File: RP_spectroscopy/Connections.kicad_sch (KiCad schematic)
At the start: 6 parts, among them J1 Extension connector 1, J2 Extension connector 2, J3 Conn_Coaxial, J4 Conn_Coaxial, J5 Conn_Coaxial, J6 Conn_Coaxial

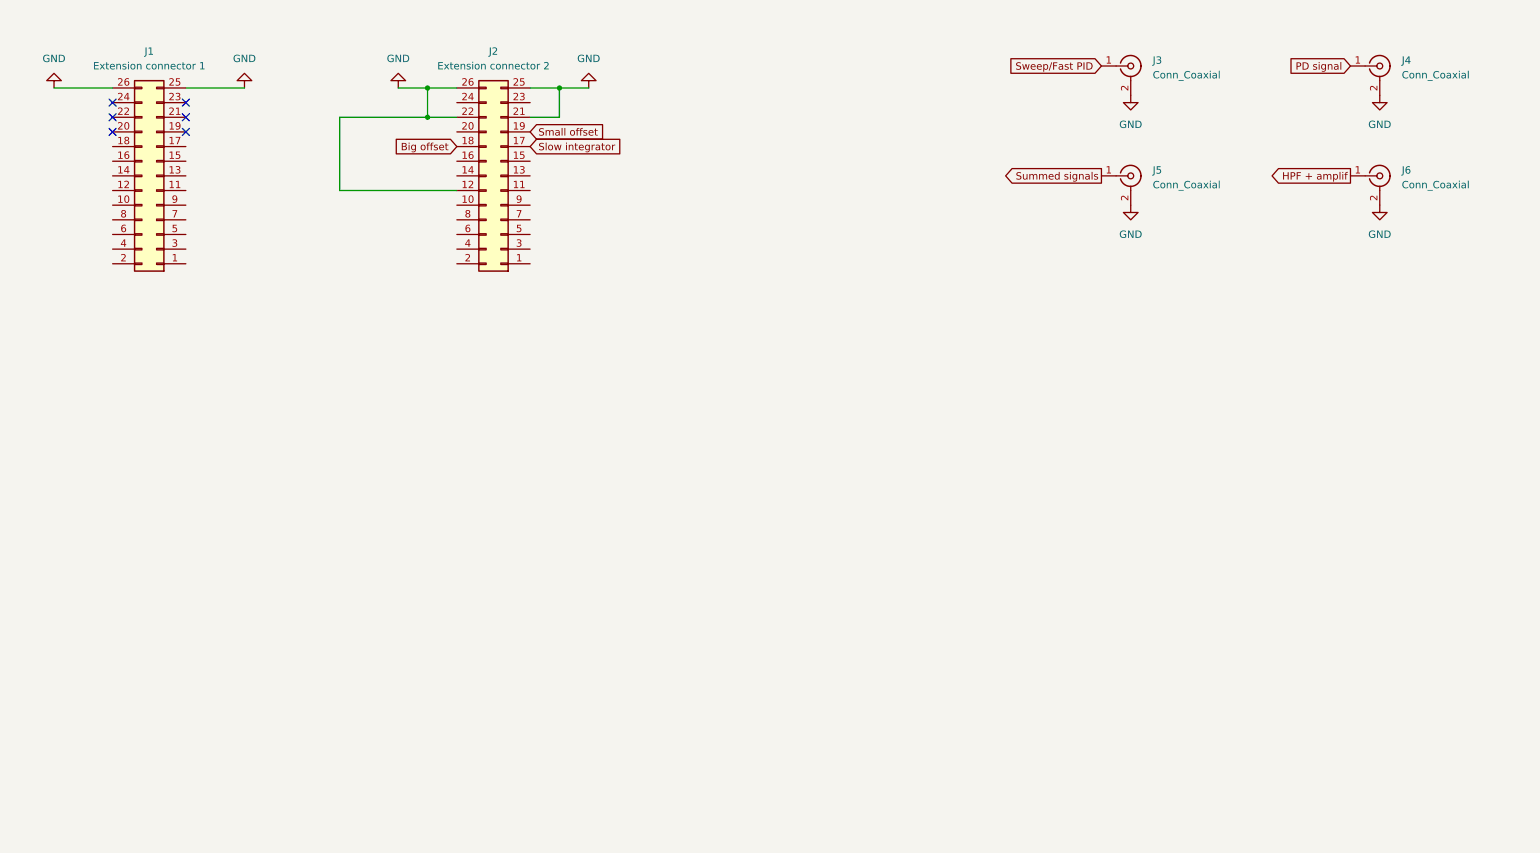
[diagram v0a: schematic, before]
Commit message: Almost finished the summator. Added also some components in the connectors schematic
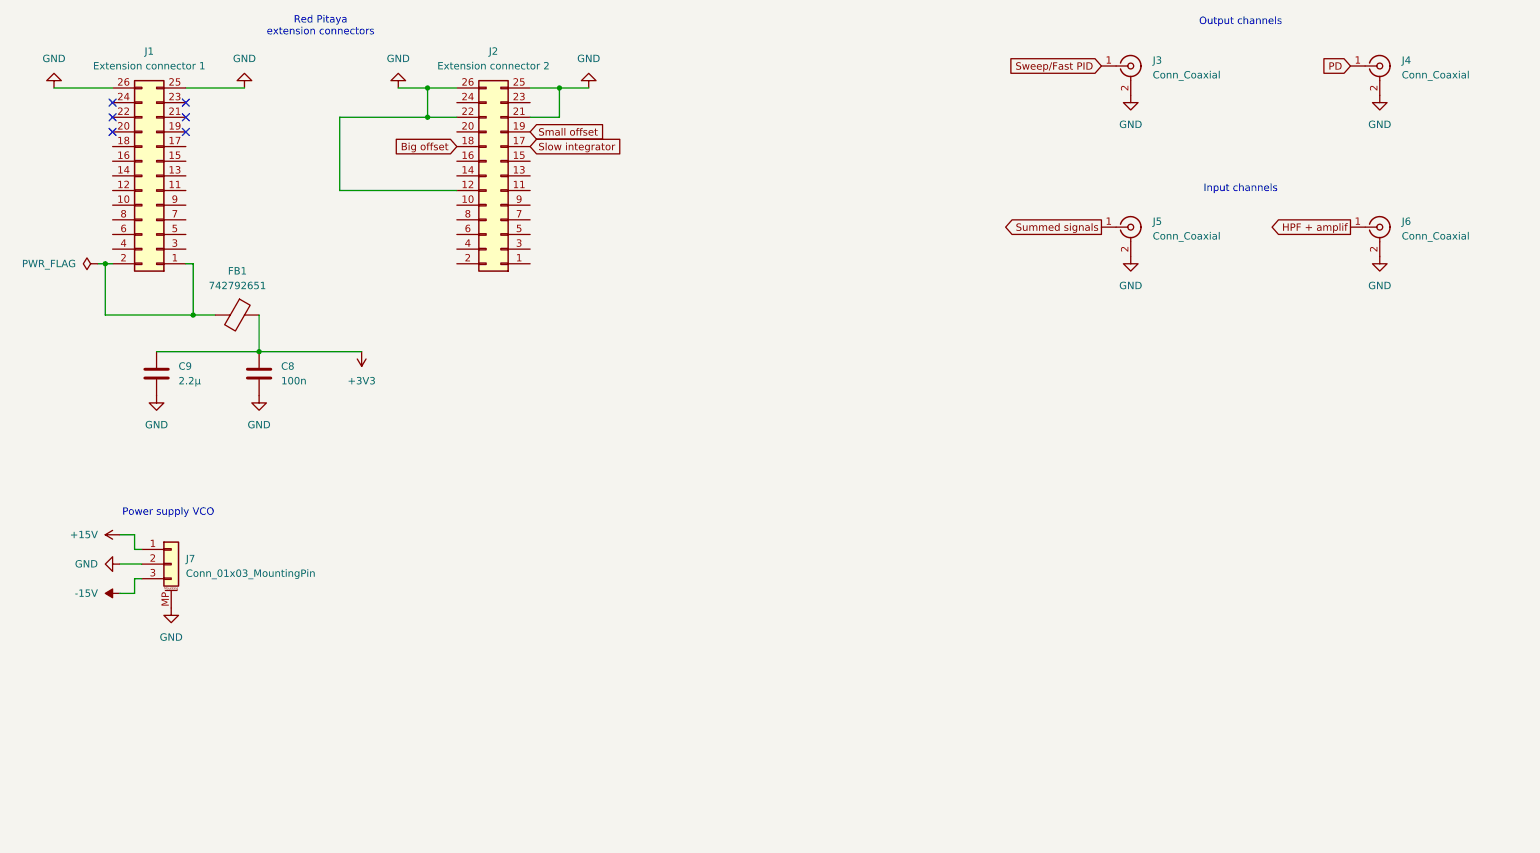
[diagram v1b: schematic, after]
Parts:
- added C8: 100n, symbol Device:C
- added C9: 2.2µ, symbol Device:C
- added FB1: 742792651, symbol Device:FerriteBead
- added J7: Conn_01x03_MountingPin, symbol Connector_Generic_MountingPin:Conn_01x03_MountingPin
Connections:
- net GND: now also C8.2, C9.2, J7.2 (Pin_2), J7.MP (MountPin)
- net at J1.1 (Pin_1): now also J1.2 (Pin_2), FB1.2
- net PD signal renamed PD
- new net +15V: J7.1 (Pin_1)
- new net +3V3: C8.1, C9.1, FB1.1
- new net -15V: J7.3 (Pin_3)
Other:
- note added: "Input channels"
- note added: "Output channels"
- note added: "Power supply VCO"
- note added: "Red Pitaya extension connectors"
- moved on the sheet: J5, J6

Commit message: Continued with the connection scheet
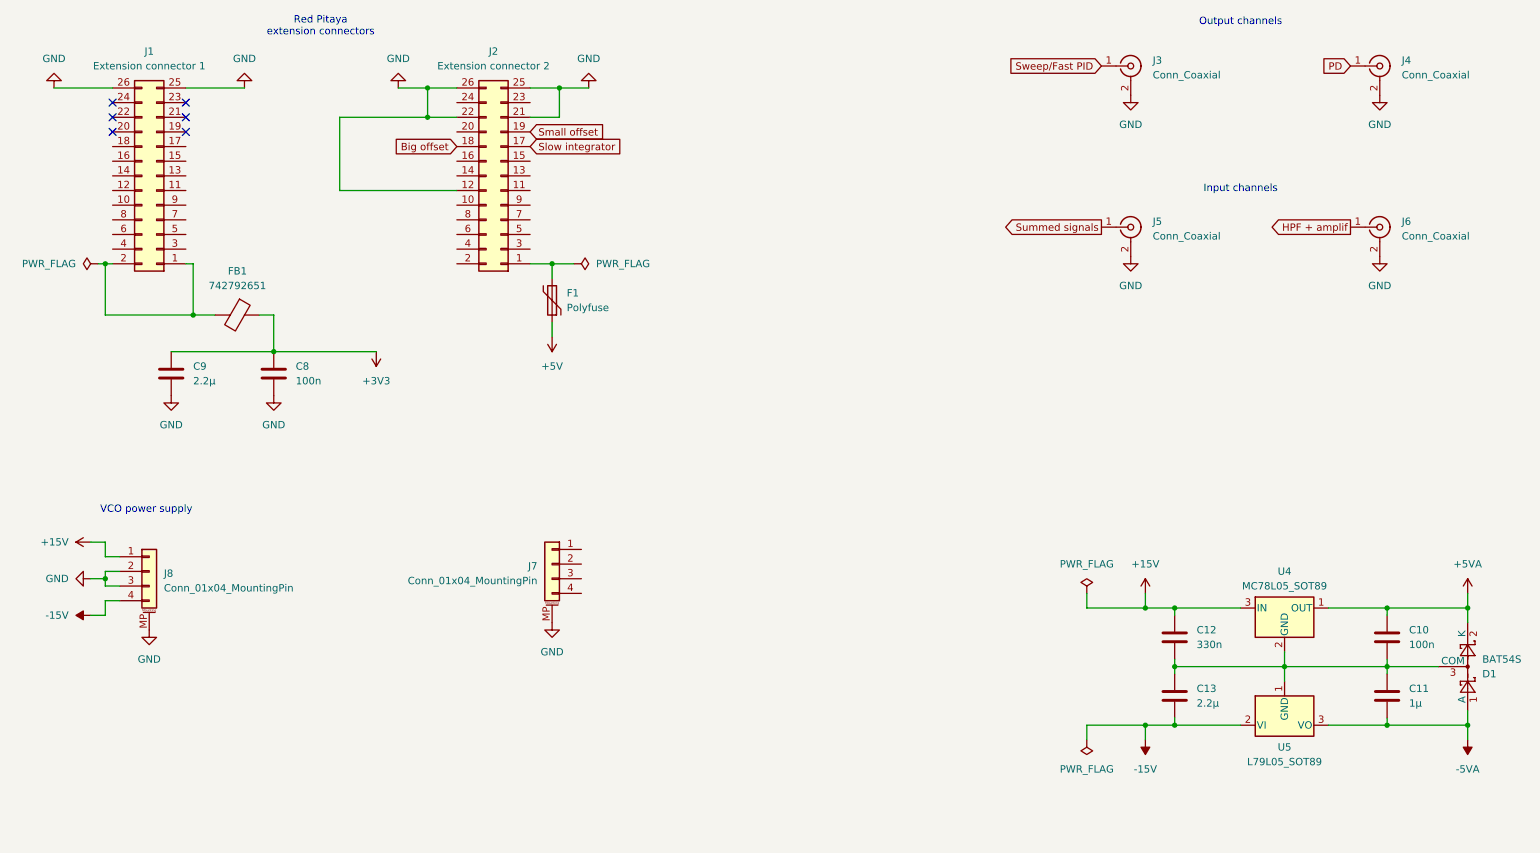
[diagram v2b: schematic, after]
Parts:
- removed J7: Conn_01x03_MountingPin, symbol Connector_Generic_MountingPin:Conn_01x03_MountingPin
- added C10: 100n, symbol Device:C
- added C11: 1µ, symbol Device:C
- added C12: 330n, symbol Device:C
- added C13: 2.2µ, symbol Device:C
- added D1: BAT54S, Package_TO_SOT_SMD:SOT-23, symbol Diode:BAT54S
- added F1: Polyfuse, symbol Device:Polyfuse
- added J7: Conn_01x04_MountingPin, symbol Connector_Generic_MountingPin:Conn_01x04_MountingPin
- added J8: Conn_01x04_MountingPin, Connector_Molex:Molex_PicoBlade_53261-0471_1x04-1MP_P1.25mm_Horizontal, symbol Connector_Generic_MountingPin:Conn_01x04_MountingPin
- added U4: MC78L05_SOT89, Package_TO_SOT_SMD:SOT-89-3_Handsoldering, symbol Regulator_Linear:MC78L05_SOT89
- added U5: L79L05_SOT89, Package_TO_SOT_SMD:SOT-89-3_Handsoldering, symbol Regulator_Linear:L79L05_SOT89
- J1, J2: footprint (none) -> Connector_PinSocket_2.54mm:PinSocket_2x13_P2.54mm_Vertical_SMD
- J3, J4, J5, J6: footprint (none) -> Connector_Coaxial:SMA_Molex_73251-1153_EdgeMount_Horizontal
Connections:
- net +15V: now also C12.1, J8.1 (Pin_1), U4.3 (IN)
- net -15V: now also C13.2, J8.4 (Pin_4), U5.2 (VI)
- net GND: now also J7.MP (MountPin), J8.2 (Pin_2), J8.3 (Pin_3), J8.MP (MountPin)
- net at J2.1 (Pin_1): now also F1.2
- new net: C10.2, C11.1, C12.2, C13.1, D1.3 (COM), U4.2 (GND), U5.1 (GND)
- new net +5V: F1.1
- new net +5VA: C10.1, D1.2 (K), U4.1 (OUT)
- new net -5VA: C11.2, D1.1 (A), U5.3 (VO)
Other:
- note added: "VCO power supply"
- note removed: "Power supply VCO"
- moved on the sheet: C8, C9

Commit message: Added components to the power supply branch. Implemented the Sallen-Key filter + amplification branch.
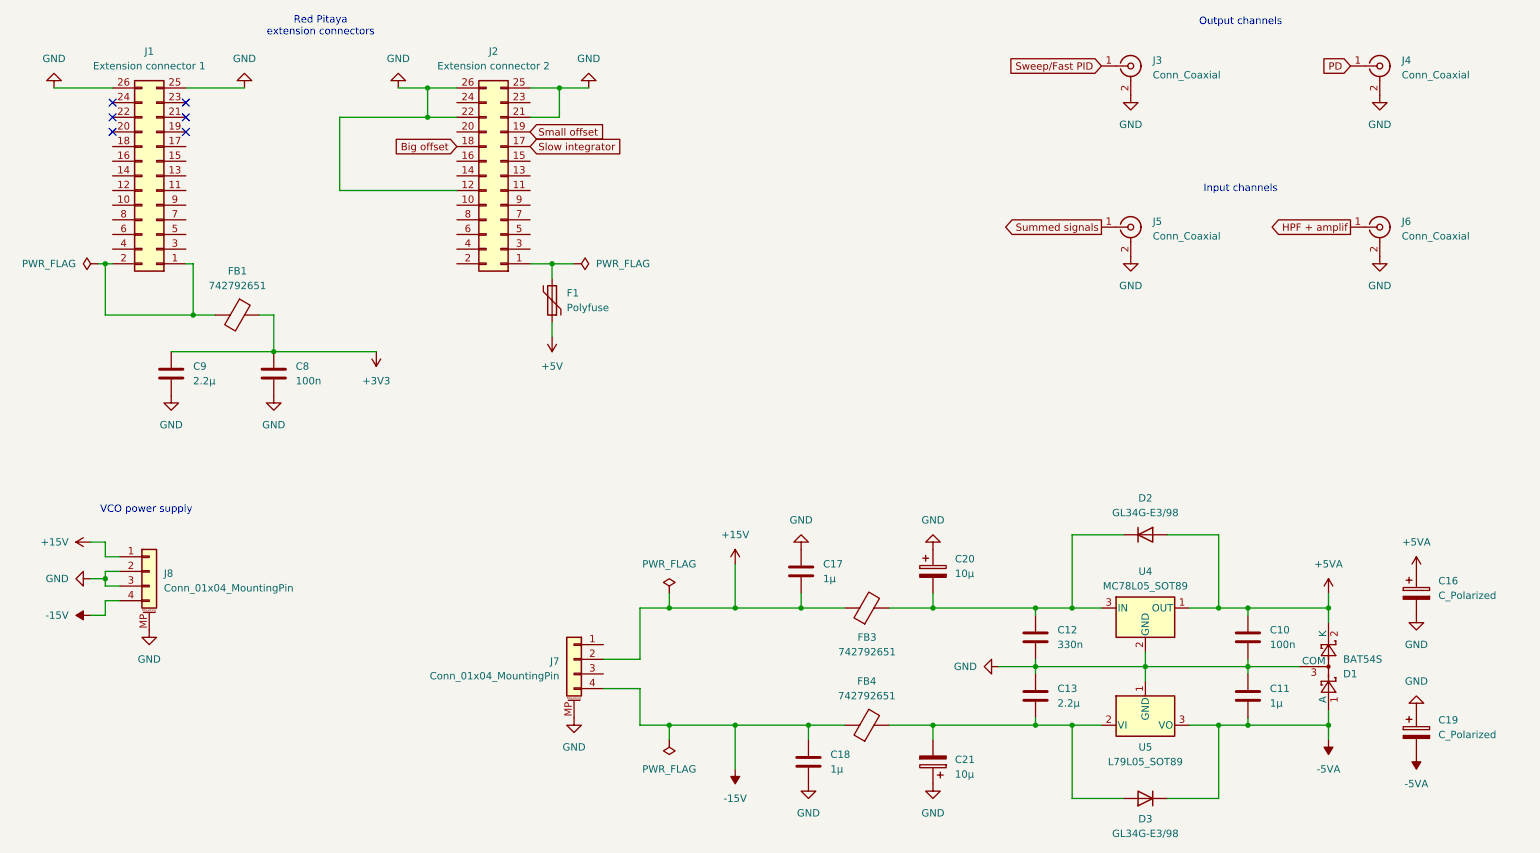
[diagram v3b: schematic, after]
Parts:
- added C16, C19: C_Polarized, symbol Device:C_Polarized
- added C17, C18: 1µ, symbol Device:C
- added C20, C21: 10µ, symbol Device:C_Polarized
- added D2, D3: GL34G-E3/98, Diode_SMD:D_MicroMELF_Handsoldering, symbol Diode:1N4148WT
- added FB3, FB4: 742792651, symbol Device:FerriteBead
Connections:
- net +15V: now also J7.2 (Pin_2), C17.2, FB3.1; no longer C12.1, U4.3 (IN)
- net +5VA: now also C16.1, D2.2 (A)
- net -15V: now also J7.4 (Pin_4), C18.1, FB4.1; no longer C13.2, U5.2 (VI)
- net -5VA: now also C19.2, D3.1 (K)
- net GND: now also C10.2, C11.1, C12.2, C13.1, D1.3 (COM), U4.2 (GND), U5.1 (GND), C16.2, C17.1, C18.2, C19.1, C20.1, C21.1
- new net: C13.2, C21.2, D3.2 (A), FB4.2, U5.2 (VI)
- new net: C12.1, C20.2, D2.1 (K), FB3.2, U4.3 (IN)
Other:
- moved on the sheet: C10, C11, C12, C13, D1, J7, U4, U5

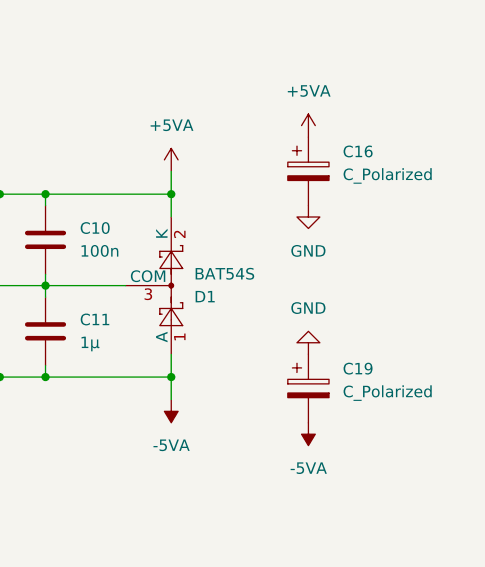
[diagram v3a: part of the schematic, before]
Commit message: Commit before deleting the VCO schematic from the main project. I have a separate project for that.
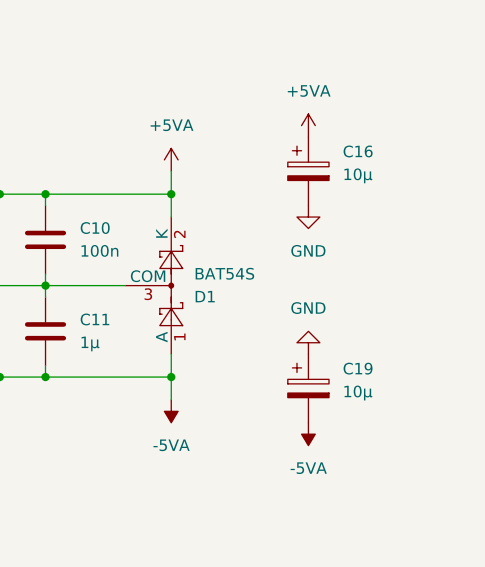
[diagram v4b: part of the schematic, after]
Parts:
- C10, C11, C12, C13, C17, C18, C8, C9: footprint (none) -> Capacitor_SMD:C_0805_2012Metric_Pad1.18x1.45mm_HandSolder
- C16, C19: value C_Polarized -> 10µ; footprint (none) -> Capacitor_SMD:CP_Elec_4x5.3
- C20, C21: footprint (none) -> Capacitor_SMD:CP_Elec_4x5.3
- F1: footprint (none) -> Fuse:Fuse_1812_4532Metric_Pad1.30x3.40mm_HandSolder
- FB1, FB3, FB4: footprint (none) -> Inductor_SMD:L_0805_2012Metric_Pad1.05x1.20mm_HandSolder
- J1, J2: footprint Connector_PinSocket_2.54mm:PinSocket_2x13_P2.54mm_Vertical_SMD -> Connector_PinSocket_2.54mm:PinSocket_2x13_P2.54mm_Vertical
- J7: footprint (none) -> Connector_Molex:Molex_PicoBlade_53261-0471_1x04-1MP_P1.25mm_Horizontal
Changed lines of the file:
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@@
 			)
 		)
-		(property "Footprint" ""
+		(property "Footprint" "Capacitor_SMD:C_0805_2012Metric_Pad1.18x1.45mm_HandSolder"
 			(at 200.3552 140.97 0)
 			(effects
@@
 			)
 		)
-		(property "Description" "Unpolarized capacitor"
+		(property "Description" "Unpolarized capacitor, 2.2µ X7R 50V"
 			(at 199.39 137.16 0)
 			(effects
@@
 			)
 		)
-		(property "Footprint" ""
+		(property "Footprint" "Inductor_SMD:L_0805_2012Metric_Pad1.05x1.20mm_HandSolder"
 			(at 170.18 144.018 90)
 			(effects
@@
 			)
 		)
-		(property "Description" "Ferrite bead"
+		(property "Description" "Ferrite bead, 742792651"
 			(at 170.18 142.24 0)
 			(effects
@@
 			)
 		)
-		(property "Description" "coaxial connector (BNC, SMA, SMB, SMC, Cinch/RCA, LEMO, ...)"
+		(property "Description" "SMA RF connector, edge mount"
 			(at 259.08 27.94 0)
 			(effects
@@
 			)
 		)
-		(property "Footprint" ""
+		(property "Footprint" "Capacitor_SMD:C_0805_2012Metric_Pad1.18x1.45mm_HandSolder"
 			(at 200.3552 130.81 0)
 			(effects
@@
 			)
 		)
-		(property "Description" "Unpolarized capacitor"
+		(property "Description" "Unpolarized capacitor, 330n X7R 50V"
 			(at 199.39 127 0)
 			(effects
@@
 			)
 		)
-		(property "Footprint" ""
+		(property "Footprint" "Capacitor_SMD:CP_Elec_4x5.3"
 			(at 182.5752 119.38 0)
 			(effects
@@
 			)
 		)
-		(property "Footprint" ""
+		(property "Footprint" "Capacitor_SMD:C_0805_2012Metric_Pad1.18x1.45mm_HandSolder"
 			(at 68.2752 85.09 0)
 			(effects
@@
 			)
 		)
-		(property "Description" "Unpolarized capacitor"
+		(property "Description" "Unpolarized capacitor, 100n X7R 50V"
 			(at 67.31 81.28 0)
 			(effects
@@
 			)
 		)
-		(property "Footprint" ""
+		(property "Footprint" "Inductor_SMD:L_0805_2012Metric_Pad1.05x1.20mm_HandSolder"
 			(at 60.96 69.342 90)
 			(effects
@@
 			)
 		)
-		(property "Description" "Ferrite bead"
+		(property "Description" "Ferrite bead, 742792651"
 			(at 60.96 71.12 0)
 			(effects
@@
 			)
 		)
-		(property "Description" "coaxial connector (BNC, SMA, SMB, SMC, Cinch/RCA, LEMO, ...)"
+		(property "Description" "SMA RF connector, edge mount"
 			(at 215.9 55.88 0)
 			(effects
@@
 			)
 		)
-		(property "Footprint" ""
+		(property "Footprint" "Capacitor_SMD:C_0805_2012Metric_Pad1.18x1.45mm_HandSolder"
 			(at 237.1852 130.81 0)
 			(effects
@@
 			)
 		)
-		(property "Description" "Unpolarized capacitor"
+		(property "Description" "Unpolarized capacitor, 100n X7R 50V"
 			(at 236.22 127 0)
 			(effects
@@
 			)
 		)
-		(property "Footprint" "Connector_PinSocket_2.54mm:PinSocket_2x13_P2.54mm_Vertical_SMD"
+		(property "Footprint" "Connector_PinSocket_2.54mm:PinSocket_2x13_P2.54mm_Vertical"
 			(at 46.99 46.99 0)
 			(effects
@@
 			)
 		)
-		(property "Footprint" ""
+		(property "Footprint" "Capacitor_SMD:CP_Elec_4x5.3"
 			(at 180.6448 144.78 0)
 			(effects
@@
 			)
 		)
-		(property "Footprint" "Connector_PinSocket_2.54mm:PinSocket_2x13_P2.54mm_Vertical_SMD"
+		(property "Footprint" "Connector_PinSocket_2.54mm:PinSocket_2x13_P2.54mm_Vertical"
 			(at 106.68 46.99 0)
 			(effects
@@
 			)
 		)
-		(property "Footprint" ""
+		(property "Footprint" "Connector_Molex:Molex_PicoBlade_53261-0471_1x04-1MP_P1.25mm_Horizontal"
 			(at 119.38 130.81 0)
 			(effects
@@
 			)
 		)
-		(property "Footprint" ""
+		(property "Footprint" "Fuse:Fuse_1812_4532Metric_Pad1.30x3.40mm_HandSolder"
 			(at 114.3 63.5 0)
 			(effects
@@
 			)
 		)
-		(property "Description" "Resettable fuse, polymeric positive temperature coefficient"
+		(property "Description" "SMDH1206B075TF / TLC-NSMD100, 2A"
 			(at 115.57 68.58 0)
 			(effects
@@
 			)
 		)
-		(property "Description" "coaxial connector (BNC, SMA, SMB, SMC, Cinch/RCA, LEMO, ...)"
+		(property "Description" "SMA RF connector, edge mount"
 			(at 259.08 55.88 0)
 			(effects
@@
 			)
 		)
-		(property "Footprint" ""
+		(property "Footprint" "Inductor_SMD:L_0805_2012Metric_Pad1.05x1.20mm_HandSolder"
 			(at 170.18 123.698 90)
 			(effects
@@
 			)
 		)
-		(property "Description" "Ferrite bead"
+		(property "Description" "Ferrite bead, 742792651"
 			(at 170.18 121.92 0)
 			(effects
@@
 			)
 		)
-		(property "Footprint" ""
+		(property "Footprint" "Capacitor_SMD:C_0805_2012Metric_Pad1.18x1.45mm_HandSolder"
 			(at 50.4952 85.09 0)
 			(effects
@@
 			)
 		)
-		(property "Description" "Unpolarized capacitor"
+		(property "Description" "Unpolarized capacitor, 2.2µ X7R 50V"
 			(at 49.53 81.28 0)
 			(effects
@@
 			)
 		)
-		(property "Value" "C_Polarized"
+		(property "Value" "10µ"
 			(at 269.24 143.8909 0)
 			(effects
@@
 			)
 		)
-		(property "Footprint" ""
+		(property "Footprint" "Capacitor_SMD:CP_Elec_4x5.3"
 			(at 266.3952 147.32 0)
 			(effects
@@
 			)
 		)
-		(property "Description" ""
+		(property "Description" "GL34G-E3/98"
 			(at 218.44 154.94 0)
 			(effects
@@
 			)
 		)
-		(property "Description" ""
+		(property "Description" "GL34G-E3/98"
 			(at 218.44 109.22 0)
 			(effects
@@
 			)
 		)
-		(property "Value" "C_Polarized"
+		(property "Value" "10µ"
 			(at 269.24 119.7609 0)
 			(effects
@@
 			)
 		)
-		(property "Footprint" ""
+		(property "Footprint" "Capacitor_SMD:CP_Elec_4x5.3"
 			(at 266.3952 123.19 0)
 			(effects
@@
 			)
 		)
-		(property "Footprint" ""
+		(property "Footprint" "Capacitor_SMD:C_0805_2012Metric_Pad1.18x1.45mm_HandSolder"
 			(at 159.7152 119.38 0)
 			(effects
@@
 			)
 		)
-		(property "Description" "Unpolarized capacitor"
+		(property "Description" "Unpolarized capacitor, 1µ X7R 50V"
 			(at 158.75 115.57 0)
 			(effects
@@
 			)
 		)
-		(property "Description" "coaxial connector (BNC, SMA, SMB, SMC, Cinch/RCA, LEMO, ...)"
+		(property "Description" "SMA RF connector, edge mount"
 			(at 215.9 27.94 0)
 			(effects
@@
 			)
 		)
-		(property "Footprint" ""
+		(property "Footprint" "Capacitor_SMD:C_0805_2012Metric_Pad1.18x1.45mm_HandSolder"
 			(at 160.9852 152.4 0)
 			(effects
@@
 			)
 		)
-		(property "Description" "Unpolarized capacitor"
+		(property "Description" "Unpolarized capacitor, 1µ X7R 50V"
 			(at 160.02 148.59 0)
 			(effects
@@
 			)
 		)
-		(property "Footprint" ""
+		(property "Footprint" "Capacitor_SMD:C_0805_2012Metric_Pad1.18x1.45mm_HandSolder"
 			(at 237.1852 140.97 0)
 			(effects
@@
 			)
 		)
-		(property "Description" "Unpolarized capacitor"
+		(property "Description" "Unpolarized capacitor, 1µ X7R 50V"
 			(at 236.22 137.16 0)
 			(effects
